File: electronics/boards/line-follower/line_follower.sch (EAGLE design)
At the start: 33 parts, among them IC1 ATTINY441-SSU, IC3 NCP1117ST50T3G, J1 GROVE_CONNECTOR2.0_1X4, J2 GROVE_CONNECTOR2.0_1X4, J3 10129383-906001ALF, Q1 TCRT5000, Q2 TCRT5000, Q3 TCRT5000, Y1 X322516MLB4SI

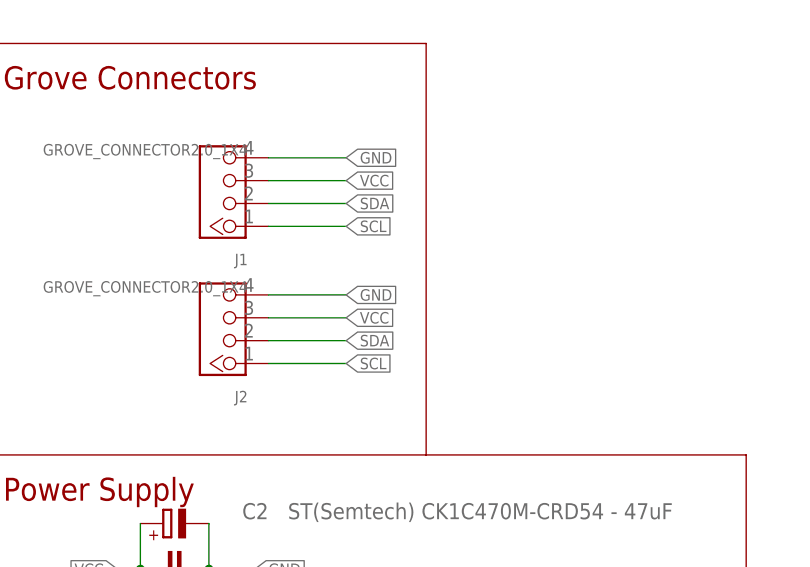
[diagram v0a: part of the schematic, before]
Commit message: - atmega-Platinen: Stop-Schicht angepasst auf Original - Attiny-Platinen: I2C-Leitungen korrigiert - CAM-Daten für alle Platinen erstellt
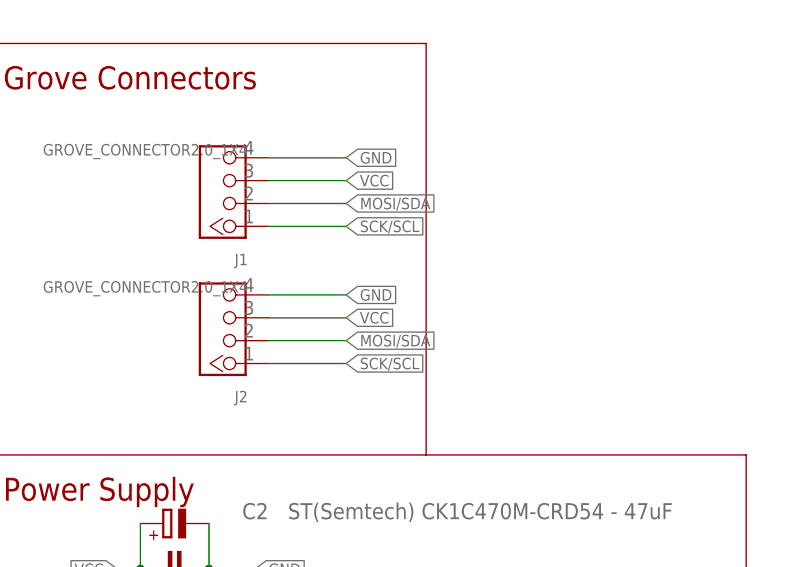
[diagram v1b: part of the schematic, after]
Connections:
- removed net SCL: J1.1, J2.1
- removed net SDA: J1.2, J2.2
- net MOSI/SDA: now also J1.2, J2.2
- net SCK/SCL: now also J1.1, J2.1
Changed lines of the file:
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@@
 </busses>
 <nets>
-<net name="SCL" class="0">
-<segment>
-<pinref part="J1" gate="G$1" pin="1"/>
-<wire x1="34.548721875" y1="88.9" x2="43.18" y2="88.9" width="0.1524" layer="91"/>
-<label x="43.18" y="88.9" size="1.27" layer="95" ratio="5" xref="yes"/>
-</segment>
-<segment>
-<pinref part="J2" gate="G$1" pin="1"/>
-<wire x1="34.548721875" y1="73.66" x2="43.18" y2="73.66" width="0.1524" layer="91"/>
-<label x="43.18" y="73.66" size="1.27" layer="95" ratio="5" xref="yes"/>
-</segment>
-</net>
-<net name="SDA" class="0">
-<segment>
-<pinref part="J1" gate="G$1" pin="2"/>
-<wire x1="34.548721875" y1="91.44" x2="43.18" y2="91.44" width="0.1524" layer="91"/>
-<label x="43.18" y="91.44" size="1.27" layer="95" ratio="5" xref="yes"/>
-</segment>
-<segment>
-<pinref part="J2" gate="G$1" pin="2"/>
-<wire x1="34.548721875" y1="76.2" x2="43.18" y2="76.2" width="0.1524" layer="91"/>
-<label x="43.18" y="76.2" size="1.27" layer="95" ratio="5" xref="yes"/>
-</segment>
-</net>
 <net name="VCC" class="0">
 <segment>
@@
 <label x="83.82" y="124.46" size="1.27" layer="95" ratio="5" rot="R180" xref="yes"/>
 </segment>
+<segment>
+<pinref part="J1" gate="G$1" pin="2"/>
+<wire x1="34.548721875" y1="91.44" x2="43.18" y2="91.44" width="0.1524" layer="91"/>
+<label x="43.18" y="91.44" size="1.27" layer="95" ratio="5" xref="yes"/>
+</segment>
+<segment>
+<pinref part="J2" gate="G$1" pin="2"/>
+<wire x1="34.548721875" y1="76.2" x2="43.18" y2="76.2" width="0.1524" layer="91"/>
+<label x="43.18" y="76.2" size="1.27" layer="95" ratio="5" xref="yes"/>
+</segment>
 </net>
 <net name="SCK/SCL" class="0">
@@
 <label x="218.44" y="127" size="1.27" layer="95" ratio="5" xref="yes"/>
 </segment>
-</net>
+<segment>
+<pinref part="J1" gate="G$1" pin="1"/>
+<wire x1="34.548721875" y1="88.9" x2="43.18" y2="88.9" width="0.1524" layer="91"/>
+<label x="43.18" y="88.9" size="1.27" layer="95" ratio="5" xref="yes"/>
+</segment>
+<segment>
+<pinref part="J2" gate="G$1" pin="1"/>
+<wire x1="34.548721875" y1="73.66" x2="43.18" y2="73.66" width="0.1524" layer="91"/>
+<label x="43.18" y="73.66" size="1.27" layer="95" ratio="5" xref="yes"/>
+</segment>
+</net>
